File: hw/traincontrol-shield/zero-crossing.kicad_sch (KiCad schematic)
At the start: 3 parts, among them U2 H11AA1

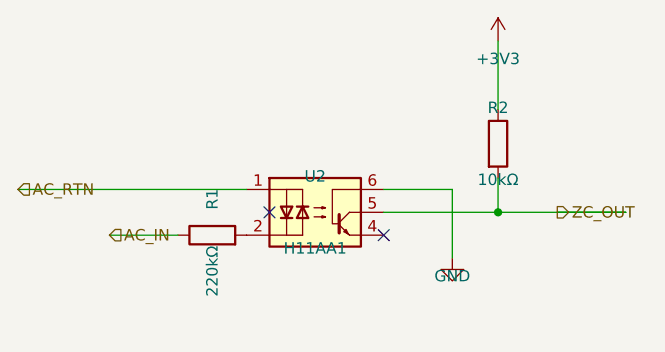
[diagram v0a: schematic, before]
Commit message: Fix U2 (H11AA1) schematic orientation for conventional NPN layout
Mirror U2 vertically (mirror x) so emitter (pin 4) is at the
bottom-right and base (pin 6) is at the top-right NC, matching
the standard NPN symbol convention (emitter → GND at bottom,
collector → pullup at centre). Also update R1, AC_IN and AC_RTN
wire/label coordinates to match the new pin positions.

Co-Authored-By: Claude Sonnet 4.6 <noreply@anthropic.com>
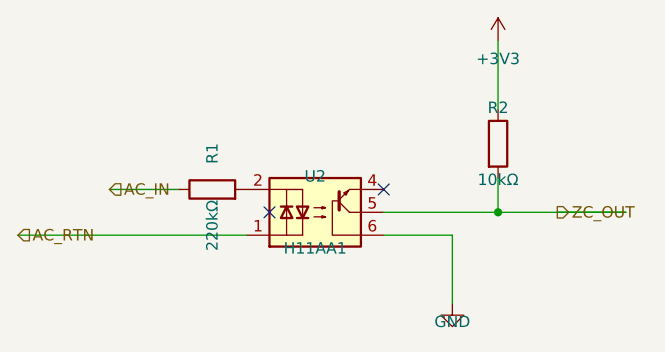
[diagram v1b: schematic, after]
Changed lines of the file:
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@@
 		(lib_id "Isolator:H11AA1")
 		(at 96.52 90.17 0)
+		(mirror x)
 		(unit 1)
 		(exclude_from_sim no)
@@
 	(symbol
 		(lib_id "Device:R")
-		(at 85.09 92.71 90)
+		(at 85.09 87.63 90)
 		(unit 1)
 		(exclude_from_sim no)
@@
 		(dnp no)
 		(property "Reference" "R1"
-			(at 85.09 88.71 0)
+			(at 85.09 83.63 0)
 			(effects (font (size 1.27 1.27)))
 		)
 		(property "Value" "220kΩ"
-			(at 85.09 96.71 0)
+			(at 85.09 91.63 0)
 			(effects (font (size 1.27 1.27)))
 		)
 		(property "Footprint" "Resistor_SMD:R_0603_1608Metric"
-			(at 85.09 92.71 0)
+			(at 85.09 87.63 0)
 			(effects (font (size 1.27 1.27)) (hide yes))
 		)
 		(property "Datasheet" "~"
-			(at 85.09 92.71 0)
+			(at 85.09 87.63 0)
 			(effects (font (size 1.27 1.27)) (hide yes))
 		)
@@
 	)
 	(wire
-		(pts (xy 104.14 87.63) (xy 111.76 87.63))
-		(stroke (width 0) (type solid))
-	)
-	(wire
-		(pts (xy 111.76 87.63) (xy 111.76 95.25))
+		(pts (xy 104.14 92.71000000000001) (xy 111.76 92.71000000000001))
+		(stroke (width 0) (type solid))
+	)
+	(wire
+		(pts (xy 111.76 92.71000000000001) (xy 111.76 100.33000000000001))
 		(stroke (width 0) (type solid))
 	)
 	(symbol
 		(lib_id "power:GND")
-		(at 111.76 95.25 0)
+		(at 111.76 100.33000000000001 0)
 		(unit 1)
 		(exclude_from_sim no)
@@
 		(dnp no)
 		(property "Reference" "#PWR0301"
-			(at 111.76 93.25 0)
+			(at 111.76 98.33000000000001 0)
 			(effects (font (size 1.27 1.27)) (hide yes))
 		)
 		(property "Value" "GND"
-			(at 111.76 97.25 0)
+			(at 111.76 102.33000000000001 0)
 			(effects (font (size 1.27 1.27)))
 		)
 		(property "Footprint" ""
-			(at 111.76 95.25 0)
+			(at 111.76 100.33000000000001 0)
 			(effects (font (size 1.27 1.27)) (hide yes))
 		)
 		(property "Datasheet" ""
-			(at 111.76 95.25 0)
+			(at 111.76 100.33000000000001 0)
 			(effects (font (size 1.27 1.27)) (hide yes))
 		)
@@
 	)
 	(wire
-		(pts (xy 88.89999999999999 87.63) (xy 71.12 87.63))
-		(stroke (width 0) (type solid))
-	)
-	(wire
-		(pts (xy 73.66 92.71) (xy 81.28 92.71))
+		(pts (xy 88.89999999999999 92.71000000000001) (xy 71.12 92.71000000000001))
+		(stroke (width 0) (type solid))
+	)
+	(wire
+		(pts (xy 73.66 87.63) (xy 81.28 87.63))
 		(stroke (width 0) (type solid))
 	)
 	(hierarchical_label "AC_IN"
 		(shape input)
-		(at 73.66 92.71 0)
+		(at 73.66 87.63 0)
 		(fields_autoplaced yes)
 		(effects (font (size 1.27 1.27)) (justify left bottom))
 		(property "Intersheetrefs" "${INTERSHEET_REFS}"
-			(at 73.66 92.71 0)
-			(effects (font (size 1.27 1.27)) (hide yes))
-		)
-	)
-	(wire
-		(pts (xy 63.50000000000001 87.63) (xy 71.12 87.63))
+			(at 73.66 87.63 0)
+			(effects (font (size 1.27 1.27)) (hide yes))
+		)
+	)
+	(wire
+		(pts (xy 63.50000000000001 92.71) (xy 71.12 92.71))
 		(stroke (width 0) (type solid))
 	)
 	(hierarchical_label "AC_RTN"
 		(shape input)
-		(at 63.50000000000001 87.63 0)
+		(at 63.50000000000001 92.71 0)
 		(fields_autoplaced yes)
 		(effects (font (size 1.27 1.27)) (justify left bottom))
 		(property "Intersheetrefs" "${INTERSHEET_REFS}"
-			(at 63.50000000000001 87.63 0)
+			(at 63.50000000000001 92.71 0)
 			(effects (font (size 1.27 1.27)) (hide yes))
 		)
@@
 	)
 	(no_connect
-		(at 104.14 92.71000000000001)
+		(at 104.14 87.63)
 	)
 	(sheet_instances
